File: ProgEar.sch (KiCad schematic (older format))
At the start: 0 parts

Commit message: Created STM32F401CBU6 component
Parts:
- added U?: STM32F401CBU6, ~, symbol STM32F401CBU6
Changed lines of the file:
@@
 EESchema Schematic File Version 2
+LIBS:stm32f401cbu6
 LIBS:power
 LIBS:device
@@
 LIBS:contrib
 LIBS:valves
+LIBS:ProgEar-cache
 EELAYER 27 0
 EELAYER END
@@
 Comment4 "This file is part of ProgEar."
 $EndDescr
+$Comp
+L STM32F401CBU6 U?
+U 1 1 54F0FA92
+P 5550 3450
+F 0 "U?" H 5550 4200 60  0000 C CNN
+F 1 "STM32F401CBU6" H 8150 1650 60  0000 C CNN
+F 2 "~" H 5550 4200 60  0000 C CNN
+F 3 "~" H 5550 4200 60  0000 C CNN
+	1    5550 3450
+	1    0    0    -1
+$EndComp
 $EndSCHEMATC

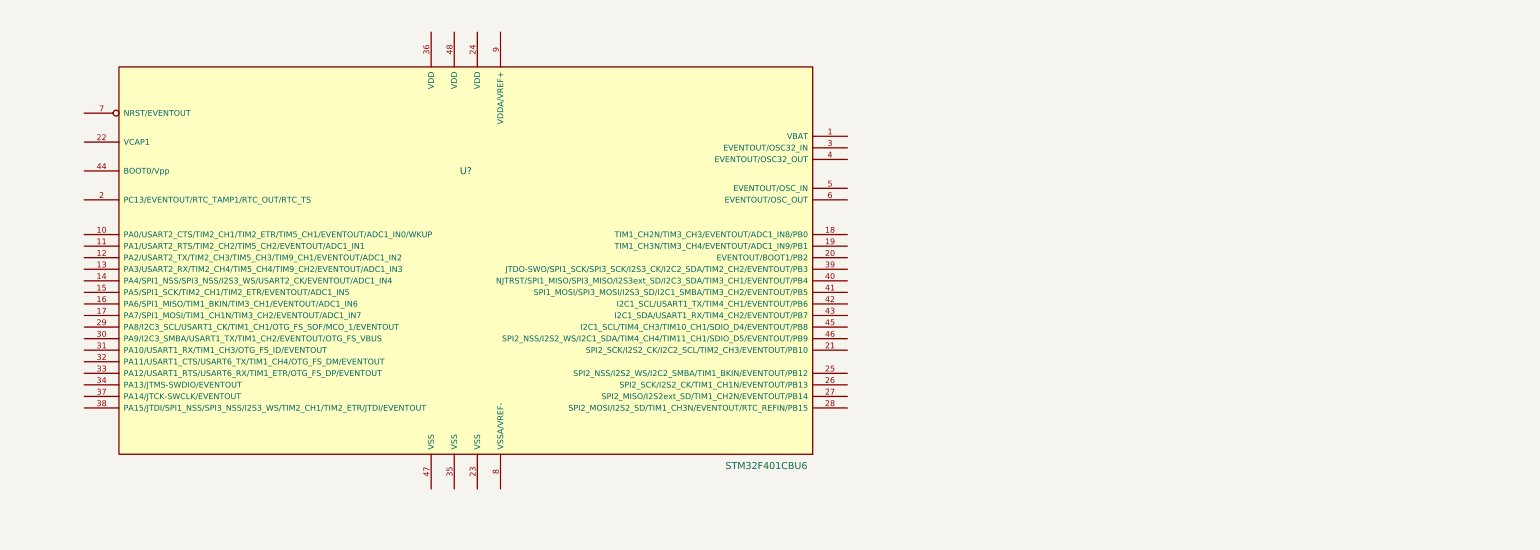
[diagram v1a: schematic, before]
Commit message: Created a library with PCM3060 component
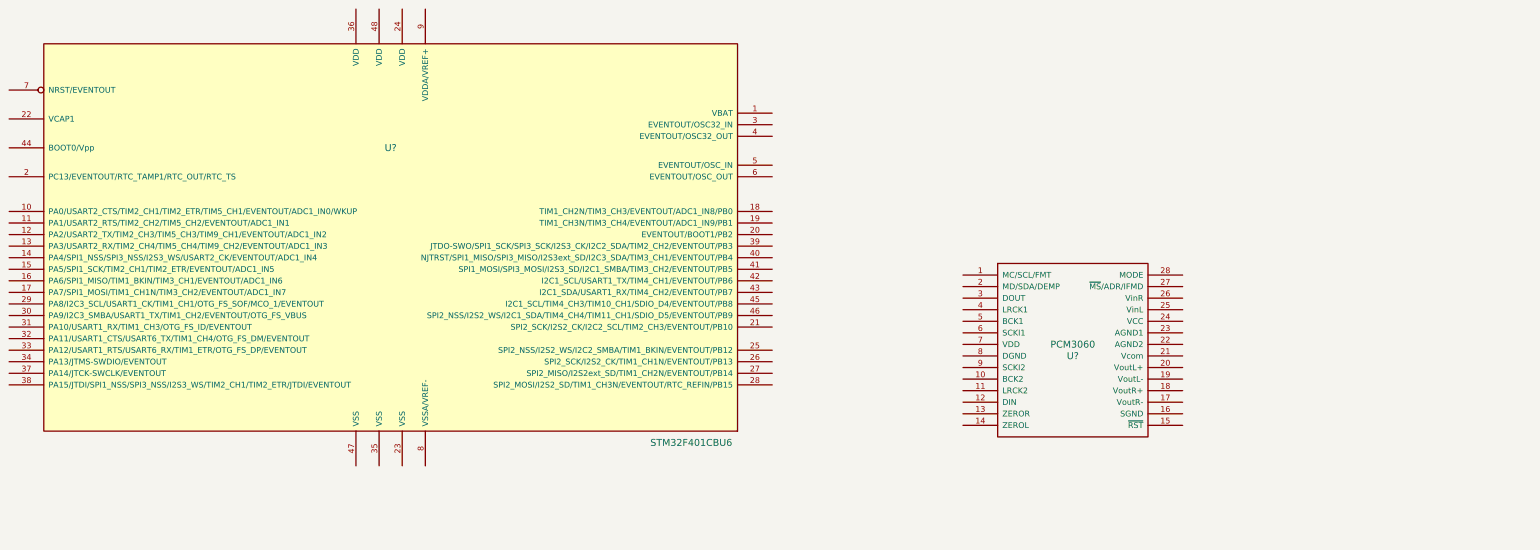
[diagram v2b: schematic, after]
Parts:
- added U?: PCM3060, ~, symbol PCM3060
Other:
- moved on the sheet: U?
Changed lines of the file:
@@
 EESchema Schematic File Version 2
 LIBS:stm32f401cbu6
+LIBS:pcm3060
 LIBS:power
 LIBS:device
@@
 L STM32F401CBU6 U?
 U 1 1 54F0FA92
-P 5550 3450
-F 0 "U?" H 5550 4200 60  0000 C CNN
-F 1 "STM32F401CBU6" H 8150 1650 60  0000 C CNN
-F 2 "~" H 5550 4200 60  0000 C CNN
-F 3 "~" H 5550 4200 60  0000 C CNN
-	1    5550 3450
+P 4900 3250
+F 0 "U?" H 4900 4000 60  0000 C CNN
+F 1 "STM32F401CBU6" H 7500 1450 60  0000 C CNN
+F 2 "~" H 4900 4000 60  0000 C CNN
+F 3 "~" H 4900 4000 60  0000 C CNN
+	1    4900 3250
 	1    0    0    -1
 $EndComp
+$Comp
+L PCM3060 U?
+U 1 1 54F2995A
+P 10800 4250
+F 0 "U?" H 10800 4200 60  0000 C CNN
+F 1 "PCM3060" H 10800 4300 60  0000 C CNN
+F 2 "~" H 10800 4200 60  0000 C CNN
+F 3 "~" H 10800 4200 60  0000 C CNN
+	1    10800 4250
+	1    0    0    -1
+$EndComp

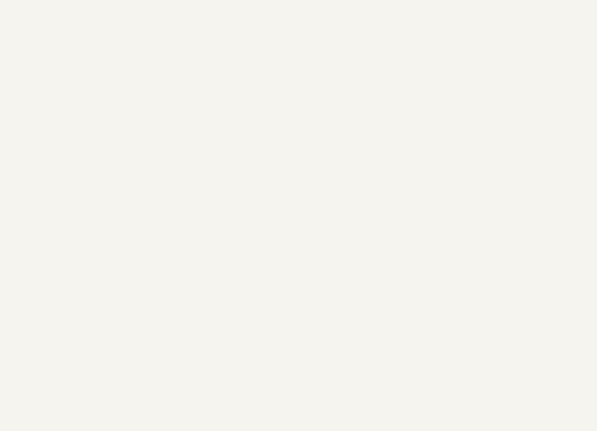
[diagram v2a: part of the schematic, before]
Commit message: Added a library with TPA1620A2 component
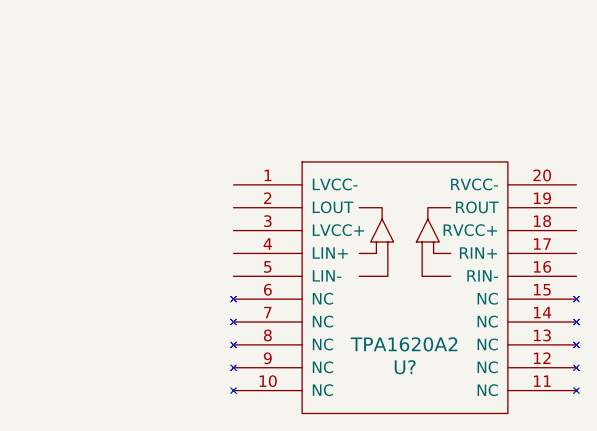
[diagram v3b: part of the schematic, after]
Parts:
- added U?: TPA1620A2, ~, symbol TPA1620A2
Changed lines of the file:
@@
 LIBS:stm32f401cbu6
 LIBS:pcm3060
+LIBS:tpa1620a2
 LIBS:power
 LIBS:device
@@
 	1    0    0    -1
 $EndComp
+$Comp
+L TPA1620A2 U?
+U 1 1 54F2A542
+P 14000 5400
+F 0 "U?" H 14000 5100 60  0000 C CNN
+F 1 "TPA1620A2" H 14000 5200 60  0000 C CNN
+F 2 "~" H 14000 5100 60  0000 C CNN
+F 3 "~" H 14000 5100 60  0000 C CNN
+	1    14000 5400
+	1    0    0    -1
+$EndComp
